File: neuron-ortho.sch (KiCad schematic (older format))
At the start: 14 parts, among them SW1 SW_PUSH, Y1 Crystal_GND24_Small

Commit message: Schema updated with ESD protection etc
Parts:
- removed C1: 1uF, symbol Device:C_Small
- removed C2, C3, C4: 0.1uF, symbol Device:C_Small
- removed C5: 10uF, symbol Device:C_Small
- removed C6: 22pF, symbol Device:C_Small
- removed SW1: SW_PUSH, symbol keyboard_parts:SW_PUSH
- removed U?: ATmega32U4-AU, Package_QFP:TQFP-44_10x10mm_P0.8mm, symbol MCU_Microchip_ATmega:ATmega32U4-AU
- removed Y1: Crystal_GND24_Small, symbol Device:Crystal_GND24_Small
- added C10, C9: 100n, symbol Device:C_Small
- added C8: 4.7n, symbol Device:C_Small
- added C? (x6): C_Small, symbol Device:C_Small
- added D1, D?: D_Small, symbol Device:D_Small
- added F1: 1A, symbol Device:Polyfuse_Small
- added J1: USB_C_Receptacle, symbol Connector:USB_C_Receptacle
- added J? (x3): Conn_01x04_Male, symbol Connector:Conn_01x04_Male
- added J?: Conn_01x06_Male, symbol Connector:Conn_01x06_Male
- added R5: 1M, symbol Device:R_Small
- added R6, R7: 22R, symbol Device:R_Small
- added U1: STM32F303C6Tx, Package_QFP:LQFP-48_7x7mm_P0.5mm, symbol MCU_ST_STM32F3:STM32F303C6Tx
- added U2: USBLC6-2SC6, Package_TO_SOT_SMD:SOT-23-6, symbol Power_Protection:USBLC6-2SC6
- added U3: NCP1117-3.3_SOT223, Package_TO_SOT_SMD:SOT-223-3_TabPin2, symbol Regulator_Linear:NCP1117-3.3_SOT223
- C7: value 22pF -> 4.7n
- R1: value 10k -> 5.1k
- R2: value 22 -> 5.1k
- R3: value 22 -> 1.5k
- R4: value 10k -> 1M
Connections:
- net labels added: 3.3V, 5V, CASE, D+Bus, D-Bus, VBUS
- net labels removed: +5V
- wire segments 43 -> 88
- no-connect marks 1 -> 10

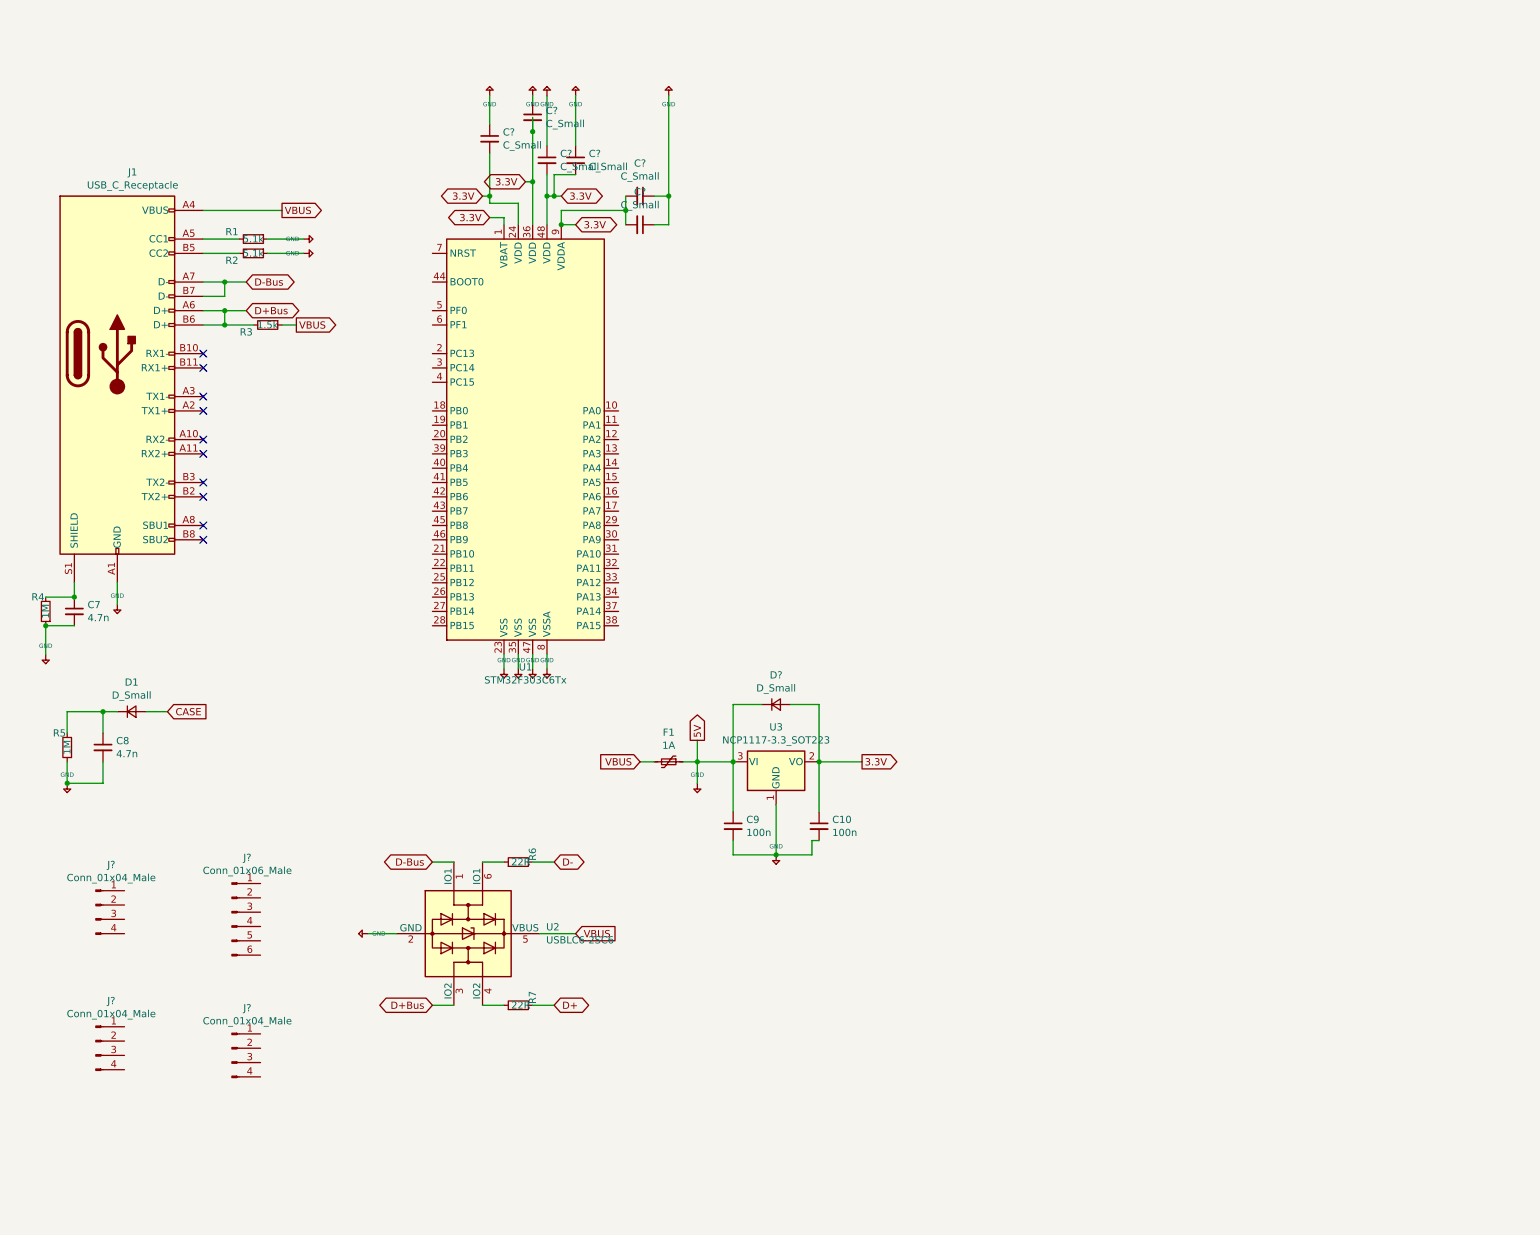
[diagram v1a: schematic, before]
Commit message: Updated schema values
Need to do switch matrix
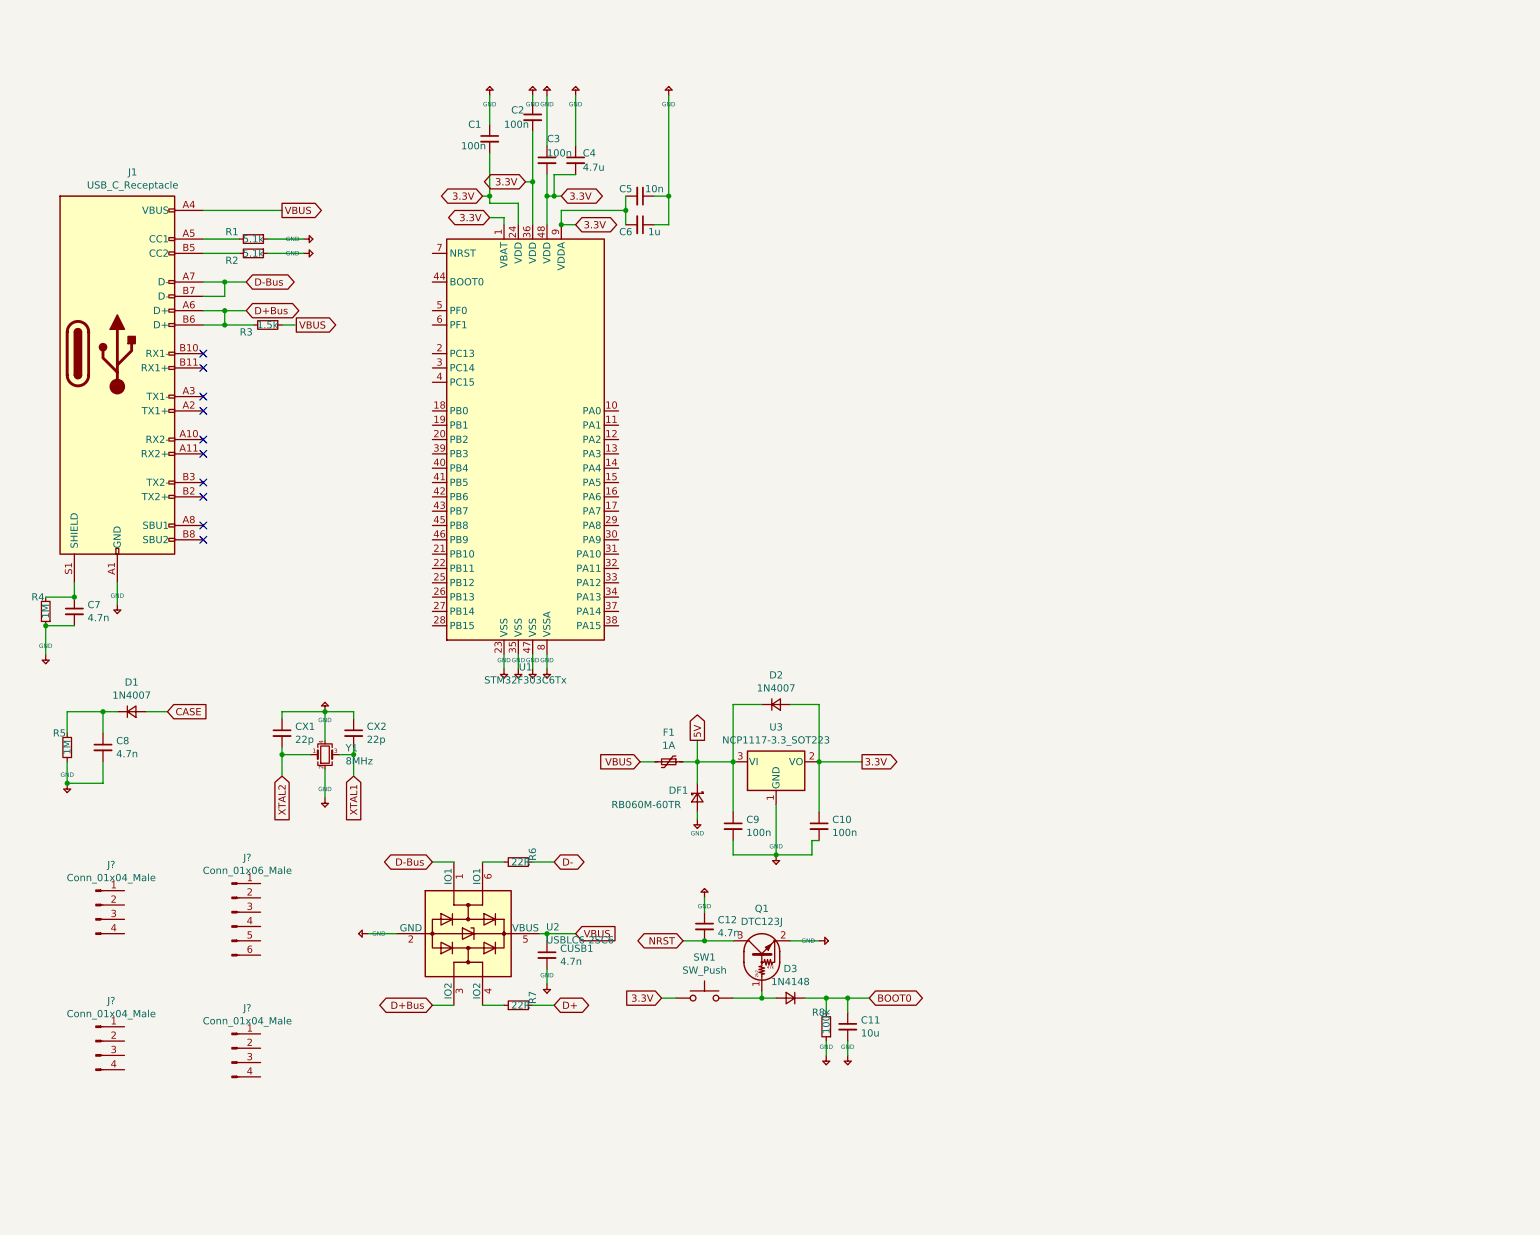
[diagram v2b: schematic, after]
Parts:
- added C11: 10u, symbol Device:C_Small
- added C12, CUSB1: 4.7n, symbol Device:C_Small
- added CX1, CX2: 22p, symbol Device:C_Small
- added D3: 1N4148, symbol Device:D_Small
- added DF1: RB060M-60TR, symbol Device:D_Schottky_Small
- added Q1: DTC123J, symbol Transistor_BJT:DTC123J
- added R8: 100k, symbol Device:R_Small
- added SW1: SW_Push, symbol Switch:SW_Push
- added Y1: 8MHz, symbol Device:Crystal_GND24_Small
- C1, C2, C3: renamed from C?; value C_Small -> 100n
- C4: renamed from C?; value C_Small -> 4.7u
- C5: renamed from C?; value C_Small -> 10n
- C6: renamed from C?; value C_Small -> 1u
- D1: value D_Small -> 1N4007
- D2: renamed from D?; value D_Small -> 1N4007
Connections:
- net +5V: now also C11.2, C12.1, CUSB1.2, CX1.1, CX2.1, DF1.2 (A), Q1.2 (E), R8.1, Y1.2, Y1.4; no longer C9.1, D2.1 (K), F1.1, U3.3 (VI)
- net 3.3V: now also SW1.1
- net VBUS: now also CUSB1.1
- new net: D3.2 (A), Q1.1 (B), SW1.2
- new net 5V: C9.1, D2.1 (K), DF1.1 (K), F1.1, U3.3 (VI)
- new net BOOT0: C11.1, D3.1 (K), R8.2
- new net NRST: C12.2, Q1.3 (C)
- new net XTAL1: CX2.2, Y1.3
- new net XTAL2: CX1.2, Y1.1

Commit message: Added Switch matrix
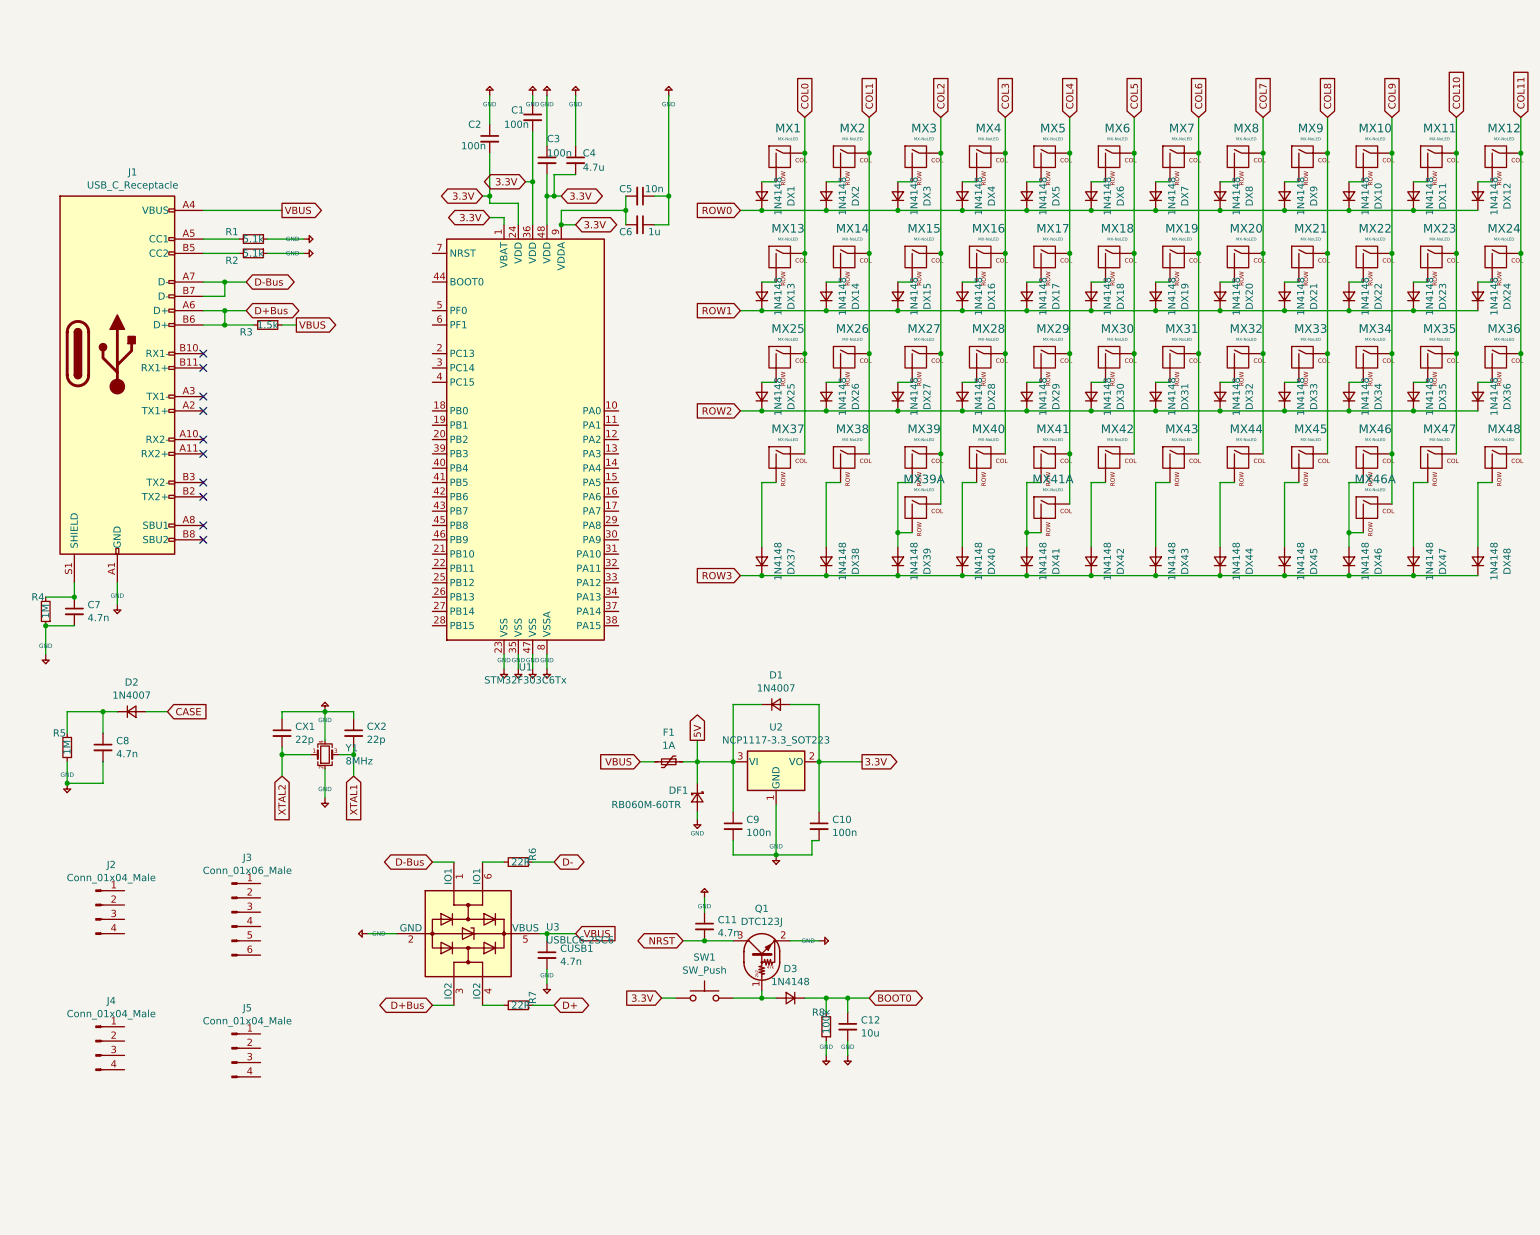
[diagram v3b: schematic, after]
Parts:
- added DX1, DX10, DX11, DX12, DX13, DX14, DX15, DX16, DX17, DX18, DX19, DX2, DX20, DX21, DX22, DX23, DX24, DX25, DX26, DX27, DX28, DX29, DX3, DX30, DX31, DX32, DX33, DX34, DX35, DX36, DX37, DX38, DX39, DX4, DX40, DX41, DX42, DX43, DX44, DX45, DX46, DX47, DX48, DX5, DX6, DX7, DX8, DX9: 1N4148, symbol Device:D_Small
- added MX1, MX10, MX11, MX12, MX13, MX14, MX15, MX16, MX17, MX18, MX19, MX2, MX20, MX21, MX22, MX23, MX24, MX25, MX26, MX27, MX28, MX29, MX3, MX30, MX31, MX32, MX33, MX34, MX35, MX36, MX37, MX38, MX39, MX39A, MX4, MX40, MX41, MX41A, MX42, MX43, MX44, MX45, MX46, MX46A, MX47, MX48, MX5, MX6, MX7, MX8, MX9: MX-NoLED, symbol MX_Alps_Hybrid:MX-NoLED
- gave numbers to parts that had none: 4
- renumbered C2 to C1, C12 to C11, C11 to C12, C1 to C2, D2 to D1, D1 to D2, U3 to U2, U2 to U3
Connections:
- new net: DX2.2 (A), MX2.2 (ROW)
- new net: DX1.2 (A), MX1.2 (ROW)
- new net: DX4.2 (A), MX4.2 (ROW)
- new net: DX6.2 (A), MX6.2 (ROW)
- new net: DX7.2 (A), MX7.2 (ROW)
- new net: DX8.2 (A), MX8.2 (ROW)
- new net: DX9.2 (A), MX9.2 (ROW)
- new net: DX10.2 (A), MX10.2 (ROW)
- new net: DX11.2 (A), MX11.2 (ROW)
- new net: DX12.2 (A), MX12.2 (ROW)
- new net: DX3.2 (A), MX3.2 (ROW)
- new net: DX5.2 (A), MX5.2 (ROW)
- new net: DX14.2 (A), MX14.2 (ROW)
- new net: DX13.2 (A), MX13.2 (ROW)
- new net: DX16.2 (A), MX16.2 (ROW)
- new net: DX18.2 (A), MX18.2 (ROW)
- new net: DX19.2 (A), MX19.2 (ROW)
- new net: DX20.2 (A), MX20.2 (ROW)
- new net: DX21.2 (A), MX21.2 (ROW)
- new net: DX22.2 (A), MX22.2 (ROW)
- new net: DX23.2 (A), MX23.2 (ROW)
- new net: DX24.2 (A), MX24.2 (ROW)
- new net: DX15.2 (A), MX15.2 (ROW)
- new net: DX17.2 (A), MX17.2 (ROW)
- new net: DX26.2 (A), MX26.2 (ROW)
- new net: DX25.2 (A), MX25.2 (ROW)
- new net: DX28.2 (A), MX28.2 (ROW)
- new net: DX30.2 (A), MX30.2 (ROW)
- new net: DX31.2 (A), MX31.2 (ROW)
- new net: DX32.2 (A), MX32.2 (ROW)
- new net: DX33.2 (A), MX33.2 (ROW)
- new net: DX34.2 (A), MX34.2 (ROW)
- new net: DX35.2 (A), MX35.2 (ROW)
- new net: DX36.2 (A), MX36.2 (ROW)
- new net: DX27.2 (A), MX27.2 (ROW)
- new net: DX29.2 (A), MX29.2 (ROW)
- new net: DX38.2 (A), MX38.2 (ROW)
- new net: DX37.2 (A), MX37.2 (ROW)
- new net: DX40.2 (A), MX40.2 (ROW)
- new net: DX42.2 (A), MX42.2 (ROW)
- new net: DX43.2 (A), MX43.2 (ROW)
- new net: DX44.2 (A), MX44.2 (ROW)
- new net: DX45.2 (A), MX45.2 (ROW)
- new net: DX46.2 (A), MX46.2 (ROW), MX46A.2 (ROW)
- new net: DX47.2 (A), MX47.2 (ROW)
- new net: DX48.2 (A), MX48.2 (ROW)
- new net: DX39.2 (A), MX39.2 (ROW), MX39A.2 (ROW)
- new net: DX41.2 (A), MX41.2 (ROW), MX41A.2 (ROW)
- new net COL0: MX1.1 (COL), MX13.1 (COL), MX25.1 (COL), MX37.1 (COL)
- new net COL1: MX14.1 (COL), MX2.1 (COL), MX26.1 (COL), MX38.1 (COL)
- new net COL10: MX11.1 (COL), MX23.1 (COL), MX35.1 (COL), MX47.1 (COL)
- new net COL11: MX12.1 (COL), MX24.1 (COL), MX36.1 (COL), MX48.1 (COL)
- new net COL2: MX15.1 (COL), MX27.1 (COL), MX3.1 (COL), MX39.1 (COL), MX39A.1 (COL)
- new net COL3: MX16.1 (COL), MX28.1 (COL), MX4.1 (COL), MX40.1 (COL)
- new net COL4: MX17.1 (COL), MX29.1 (COL), MX41.1 (COL), MX41A.1 (COL), MX5.1 (COL)
- new net COL5: MX18.1 (COL), MX30.1 (COL), MX42.1 (COL), MX6.1 (COL)
- new net COL6: MX19.1 (COL), MX31.1 (COL), MX43.1 (COL), MX7.1 (COL)
- new net COL7: MX20.1 (COL), MX32.1 (COL), MX44.1 (COL), MX8.1 (COL)
- new net COL8: MX21.1 (COL), MX33.1 (COL), MX45.1 (COL), MX9.1 (COL)
- new net COL9: MX10.1 (COL), MX22.1 (COL), MX34.1 (COL), MX46.1 (COL), MX46A.1 (COL)
- new net ROW0: DX1.1 (K), DX10.1 (K), DX11.1 (K), DX12.1 (K), DX2.1 (K), DX3.1 (K), DX4.1 (K), DX5.1 (K), DX6.1 (K), DX7.1 (K), DX8.1 (K), DX9.1 (K)
- new net ROW1: DX13.1 (K), DX14.1 (K), DX15.1 (K), DX16.1 (K), DX17.1 (K), DX18.1 (K), DX19.1 (K), DX20.1 (K), DX21.1 (K), DX22.1 (K), DX23.1 (K), DX24.1 (K)
- new net ROW2: DX25.1 (K), DX26.1 (K), DX27.1 (K), DX28.1 (K), DX29.1 (K), DX30.1 (K), DX31.1 (K), DX32.1 (K), DX33.1 (K), DX34.1 (K), DX35.1 (K), DX36.1 (K)
- new net ROW3: DX37.1 (K), DX38.1 (K), DX39.1 (K), DX40.1 (K), DX41.1 (K), DX42.1 (K), DX43.1 (K), DX44.1 (K), DX45.1 (K), DX46.1 (K), DX47.1 (K), DX48.1 (K)

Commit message: Assigned some MCU pins
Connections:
- net +5V: now also J2.4 (Pin_4), J3.1 (Pin_1)
- net 3.3V: now also J3.6 (Pin_6)
- net 5V: now also J2.1 (Pin_1)
- net BOOT0: now also J3.3 (Pin_3), U1.44 (BOOT0)
- net NRST: now also J3.2 (Pin_2), U1.7 (NRST)
- net XTAL1: now also U1.5 (PF0)
- net XTAL2: now also U1.6 (PF1)
- net SDA: now reaches J2.2 (Pin_2)
- net SCL: now reaches J2.3 (Pin_3)
- net SWDIO: now reaches J3.4 (Pin_4)
- net SWCLK: now reaches J3.5 (Pin_5)
- net Extra1: now reaches J4.1 (Pin_1)
- net Extra2: now reaches J4.2 (Pin_2)
- net Extra3: now reaches J4.3 (Pin_3)
- net Extra4: now reaches J4.4 (Pin_4)
- net Extra5: now reaches J5.1 (Pin_1)
- net Extra6: now reaches J5.2 (Pin_2)
- net Extra7: now reaches J5.3 (Pin_3)
- net Extra8: now reaches J5.4 (Pin_4)
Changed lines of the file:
@@
 Wire Wire Line
 	6600 2700 6700 2700
+Text GLabel 3250 1800 0    50   Input ~ 0
+NRST
+Wire Wire Line
+	3350 1800 3250 1800
+Wire Wire Line
+	3250 2000 3350 2000
+Text GLabel 3250 2200 0    50   Input ~ 0
+XTAL1
+Text GLabel 3250 2300 0    50   Input ~ 0
+XTAL2
+Wire Wire Line
+	3250 2200 3350 2200
+Wire Wire Line
+	3350 2300 3250 2300
+Text GLabel 4800 4000 2    50   BiDi ~ 0
+D-
+Text GLabel 4800 4100 2    50   BiDi ~ 0
+D+
+Text GLabel 3250 2500 0    50   Input ~ 0
+COL0
+Text GLabel 3250 2600 0    50   Input ~ 0
+COL1
+Text GLabel 3250 2700 0    50   Input ~ 0
+COL2
+Text GLabel 2600 3100 0    50   Input ~ 0
+ROW0
+Text GLabel 2600 3200 0    50   Input ~ 0
+ROW1
+Text GLabel 2600 3300 0    50   Input ~ 0
+ROW2
+Text GLabel 2600 3400 0    50   Input ~ 0
+ROW3
+Text GLabel 4850 2450 2    50   Input ~ 0
+COL3
+Text GLabel 4850 2600 2    50   Input ~ 0
+COL4
+Text GLabel 4850 2750 2    50   Input ~ 0
+COL5
+Text GLabel 4850 2900 2    50   Input ~ 0
+COL6
+Text GLabel 4850 3050 2    50   Input ~ 0
+COL7
+Text GLabel 4850 3200 2    50   Input ~ 0
+COL8
+Text GLabel 4850 3350 2    50   Input ~ 0
+COL9
+Text GLabel 4850 3500 2    50   Input ~ 0
+COL10
+Text GLabel 4850 3650 2    50   Input ~ 0
+COL11
+$Comp
+L keyboard_parts:GND #PWR?
+U 1 1 5E796914
+P 1350 6550
+F 0 "#PWR?" H 1350 6600 20  0001 C CNN
+F 1 "GND" H 1350 6609 30  0000 C CNN
+F 2 "" H 1350 6550 60  0000 C CNN
+F 3 "" H 1350 6550 60  0000 C CNN
+	1    1350 6550
+	0    -1   -1   0
+$EndComp
+$Comp
+L keyboard_parts:GND #PWR?
+U 1 1 5E79741B
+P 2300 6200
+F 0 "#PWR?" H 2300 6250 20  0001 C CNN
+F 1 "GND" H 2300 6259 30  0000 C CNN
+F 2 "" H 2300 6200 60  0000 C CNN
+F 3 "" H 2300 6200 60  0000 C CNN
+	1    2300 6200
+	0    -1   -1   0
+$EndComp
+Text GLabel 1350 6250 2    50   Input ~ 0
+5V
+Text GLabel 1350 6350 2    50   Input ~ 0
+SDA
+Text GLabel 1350 6450 2    50   Input ~ 0
+SCL
+Text GLabel 2300 6300 2    50   Input ~ 0
+NRST
+Text GLabel 2300 6400 2    50   Input ~ 0
+BOOT0
+Text GLabel 2300 6500 2    50   Input ~ 0
+SWDIO
+Text GLabel 2300 6600 2    50   Input ~ 0
+SWCLK
+Text GLabel 2300 6700 2    50   Input ~ 0
+3.3V
+Text GLabel 2250 7250 2    50   Input ~ 0
+Extra5
+Text GLabel 2250 7350 2    50   Input ~ 0
+Extra6
+Text GLabel 2250 7450 2    50   Input ~ 0
+Extra7
+Text GLabel 2250 7550 2    50   Input ~ 0
+Extra8
+Text GLabel 1300 7200 2    50   Input ~ 0
+Extra1
+Text GLabel 1300 7300 2    50   Input ~ 0
+Extra2
+Text GLabel 1300 7400 2    50   Input ~ 0
+Extra3
+Text GLabel 1300 7500 2    50   Input ~ 0
+Extra4
+Wire Wire Line
+	1200 6250 1350 6250
+Wire Wire Line
+	1200 6350 1350 6350
+Wire Wire Line
+	1200 6450 1350 6450
+Wire Wire Line
+	1200 6550 1350 6550
+Wire Wire Line
+	2150 6200 2300 6200
+Wire Wire Line
+	2150 6300 2300 6300
+Wire Wire Line
+	2150 6400 2300 6400
+Wire Wire Line
+	2150 6500 2300 6500
+Wire Wire Line
+	2150 6600 2300 6600
+Wire Wire Line
+	2150 6700 2300 6700
+Wire Wire Line
+	1200 7200 1300 7200
+Wire Wire Line
+	1200 7300 1300 7300
+Wire Wire Line
+	1200 7400 1300 7400
+Wire Wire Line
+	1200 7500 1300 7500
+Wire Wire Line
+	2150 7250 2250 7250
+Wire Wire Line
+	2150 7350 2250 7350
+Wire Wire Line
+	2150 7450 2250 7450
+Wire Wire Line
+	2150 7550 2250 7550
+Text GLabel 3250 2000 0    50   Input ~ 0
+BOOT0
+Text GLabel 4950 4250 2    50   Input ~ 0
+SWDIO
+Text GLabel 4950 4400 2    50   Input ~ 0
+SWCLK
+Text GLabel 4850 3800 2    50   Input ~ 0
+SDA
+Text GLabel 4850 3900 2    50   Input ~ 0
+SCL
+Text GLabel 2650 3650 0    50   Input ~ 0
+Extra1
+Text GLabel 2650 3800 0    50   Input ~ 0
+Extra2
+Text GLabel 2350 4000 2    50   Input ~ 0
+Extra3
+Text GLabel 2350 4100 2    50   Input ~ 0
+Extra4
+Text GLabel 2350 4200 2    50   Input ~ 0
+Extra5
+Text GLabel 2350 4300 2    50   Input ~ 0
+Extra6
+Text GLabel 2350 4400 2    50   Input ~ 0
+Extra7
+Text GLabel 2350 4500 2    50   Input ~ 0
+Extra8
 $EndSCHEMATC
